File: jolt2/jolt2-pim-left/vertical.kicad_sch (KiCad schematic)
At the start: 4 parts, among them J13 Conn_01x02_Pin, J14 Conn_01x02_Pin, J15 Conn_01x02_Pin, J16 Conn_01x02_Pin

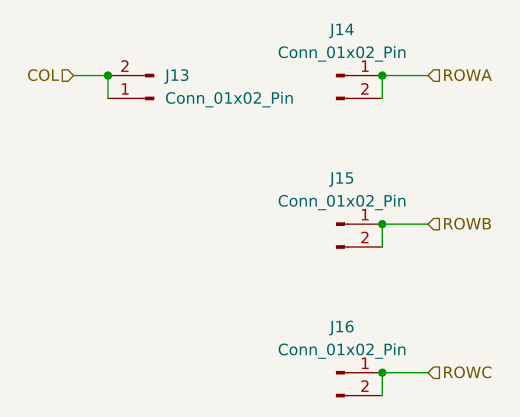
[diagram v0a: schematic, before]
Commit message: jolt2-pim-left: Finalize routing
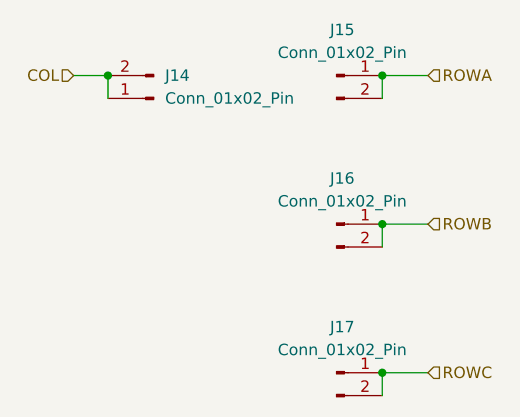
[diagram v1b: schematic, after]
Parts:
- renumbered J13 to J14, J14 to J15, J15 to J16, J16 to J17
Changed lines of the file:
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@@
 		(dnp no)
 		(fields_autoplaced yes)
-		(property "Reference" "J15"
+		(property "Reference" "J16"
 			(at 60.325 63.5 0)
 			(effects
@@
 			(project ""
 				(path "/5e404b8e-7f18-4204-bb67-87c83d2db771/029d86d1-e5b3-4172-a8dd-479e089a0442"
-					(reference "J15")
+					(reference "J16")
 					(unit 1)
 				)
 				(path "/5e404b8e-7f18-4204-bb67-87c83d2db771/17b916f7-ebfc-4d6b-a00a-a1c2400a1083"
-					(reference "J3")
+					(reference "J4")
 					(unit 1)
 				)
 				(path "/5e404b8e-7f18-4204-bb67-87c83d2db771/3ff70a16-bd04-4e60-bc61-4e3e1bf429cd"
-					(reference "J7")
+					(reference "J8")
 					(unit 1)
 				)
 				(path "/5e404b8e-7f18-4204-bb67-87c83d2db771/42146c1c-342d-4727-8b3f-2f54e7f84a3f"
-					(reference "J11")
+					(reference "J12")
 					(unit 1)
 				)
 				(path "/5e404b8e-7f18-4204-bb67-87c83d2db771/c6e71873-f81a-4892-a219-f7518ad6cce9"
-					(reference "J23")
+					(reference "J24")
 					(unit 1)
 				)
 				(path "/5e404b8e-7f18-4204-bb67-87c83d2db771/db596c9f-6bee-4ab9-b1c0-0cb65b9b558f"
-					(reference "J19")
+					(reference "J20")
 					(unit 1)
 				)
 				(path "/5e404b8e-7f18-4204-bb67-87c83d2db771/e95bee69-4f13-400e-8392-2bce6da6b398"
-					(reference "J27")
+					(reference "J28")
 					(unit 1)
 				)
@@
 		(dnp no)
 		(fields_autoplaced yes)
-		(property "Reference" "J14"
+		(property "Reference" "J15"
 			(at 60.325 46.99 0)
 			(effects
@@
 			(project ""
 				(path "/5e404b8e-7f18-4204-bb67-87c83d2db771/029d86d1-e5b3-4172-a8dd-479e089a0442"
-					(reference "J14")
+					(reference "J15")
 					(unit 1)
 				)
 				(path "/5e404b8e-7f18-4204-bb67-87c83d2db771/17b916f7-ebfc-4d6b-a00a-a1c2400a1083"
-					(reference "J2")
+					(reference "J3")
 					(unit 1)
 				)
 				(path "/5e404b8e-7f18-4204-bb67-87c83d2db771/3ff70a16-bd04-4e60-bc61-4e3e1bf429cd"
-					(reference "J6")
+					(reference "J7")
 					(unit 1)
 				)
 				(path "/5e404b8e-7f18-4204-bb67-87c83d2db771/42146c1c-342d-4727-8b3f-2f54e7f84a3f"
-					(reference "J10")
+					(reference "J11")
 					(unit 1)
 				)
 				(path "/5e404b8e-7f18-4204-bb67-87c83d2db771/c6e71873-f81a-4892-a219-f7518ad6cce9"
-					(reference "J22")
+					(reference "J23")
 					(unit 1)
 				)
 				(path "/5e404b8e-7f18-4204-bb67-87c83d2db771/db596c9f-6bee-4ab9-b1c0-0cb65b9b558f"
-					(reference "J18")
+					(reference "J19")
 					(unit 1)
 				)
 				(path "/5e404b8e-7f18-4204-bb67-87c83d2db771/e95bee69-4f13-400e-8392-2bce6da6b398"
-					(reference "J26")
+					(reference "J27")
 					(unit 1)
 				)
@@
 		(dnp no)
 		(fields_autoplaced yes)
-		(property "Reference" "J16"
+		(property "Reference" "J17"
 			(at 60.325 80.01 0)
 			(effects
@@
 			(project ""
 				(path "/5e404b8e-7f18-4204-bb67-87c83d2db771/029d86d1-e5b3-4172-a8dd-479e089a0442"
-					(reference "J16")
+					(reference "J17")
 					(unit 1)
 				)
 				(path "/5e404b8e-7f18-4204-bb67-87c83d2db771/17b916f7-ebfc-4d6b-a00a-a1c2400a1083"
-					(reference "J4")
+					(reference "J5")
 					(unit 1)
 				)
 				(path "/5e404b8e-7f18-4204-bb67-87c83d2db771/3ff70a16-bd04-4e60-bc61-4e3e1bf429cd"
-					(reference "J8")
+					(reference "J9")
 					(unit 1)
 				)
 				(path "/5e404b8e-7f18-4204-bb67-87c83d2db771/42146c1c-342d-4727-8b3f-2f54e7f84a3f"
-					(reference "J12")
+					(reference "J13")
 					(unit 1)
 				)
 				(path "/5e404b8e-7f18-4204-bb67-87c83d2db771/c6e71873-f81a-4892-a219-f7518ad6cce9"
-					(reference "J24")
+					(reference "J25")
 					(unit 1)
 				)
 				(path "/5e404b8e-7f18-4204-bb67-87c83d2db771/db596c9f-6bee-4ab9-b1c0-0cb65b9b558f"
-					(reference "J20")
+					(reference "J21")
 					(unit 1)
 				)
 				(path "/5e404b8e-7f18-4204-bb67-87c83d2db771/e95bee69-4f13-400e-8392-2bce6da6b398"
-					(reference "J28")
+					(reference "J29")
 					(unit 1)
 				)
@@
 		(dnp no)
 		(fields_autoplaced yes)
-		(property "Reference" "J13"
+		(property "Reference" "J14"
 			(at 40.64 52.0699 0)
 			(effects
@@
 			(project ""
 				(path "/5e404b8e-7f18-4204-bb67-87c83d2db771/029d86d1-e5b3-4172-a8dd-479e089a0442"
-					(reference "J13")
+					(reference "J14")
 					(unit 1)
 				)
 				(path "/5e404b8e-7f18-4204-bb67-87c83d2db771/17b916f7-ebfc-4d6b-a00a-a1c2400a1083"
-					(reference "J1")
+					(reference "J2")
 					(unit 1)
 				)
 				(path "/5e404b8e-7f18-4204-bb67-87c83d2db771/3ff70a16-bd04-4e60-bc61-4e3e1bf429cd"
-					(reference "J5")
+					(reference "J6")
 					(unit 1)
 				)
 				(path "/5e404b8e-7f18-4204-bb67-87c83d2db771/42146c1c-342d-4727-8b3f-2f54e7f84a3f"
-					(reference "J9")
+					(reference "J10")
 					(unit 1)
 				)
 				(path "/5e404b8e-7f18-4204-bb67-87c83d2db771/c6e71873-f81a-4892-a219-f7518ad6cce9"
-					(reference "J21")
+					(reference "J22")
 					(unit 1)
 				)
 				(path "/5e404b8e-7f18-4204-bb67-87c83d2db771/db596c9f-6bee-4ab9-b1c0-0cb65b9b558f"
-					(reference "J17")
+					(reference "J18")
 					(unit 1)
 				)
 				(path "/5e404b8e-7f18-4204-bb67-87c83d2db771/e95bee69-4f13-400e-8392-2bce6da6b398"
-					(reference "J25")
-					(unit 1)
-				)
+					(reference "J26")
+					(unit 1)
+				)
